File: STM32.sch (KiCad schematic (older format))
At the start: 46 parts, among them J1 Conn_02x05_Odd_Even, J2 Conn_02x03_Odd_Even, J3 Conn_01x30_Male, J4 Conn_02x03_Odd_Even, J5 Conn_01x30_Male, SW1 SW_Push, SW2 SW_Push, SW3 SW_Push, U1 LD1117S33TR_SOT223, U2 STM32F091RCTx, X1 32.768kHz(12.5pF), X2 8MHz(20pF)

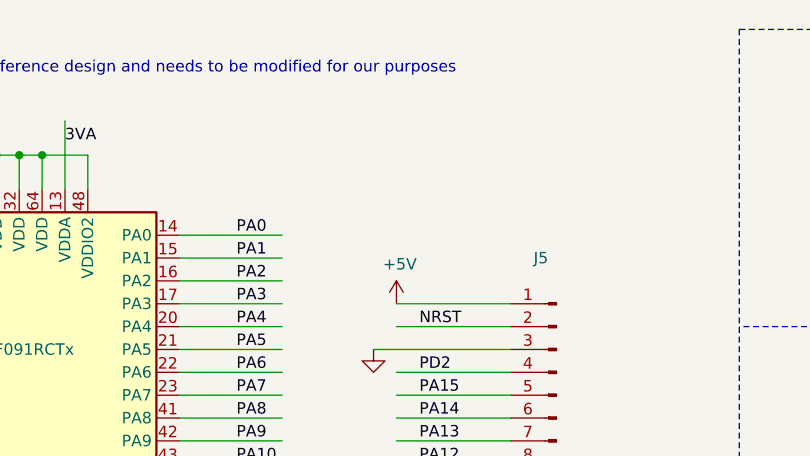
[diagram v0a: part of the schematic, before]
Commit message: updated the readme and added example of heirarchical labels
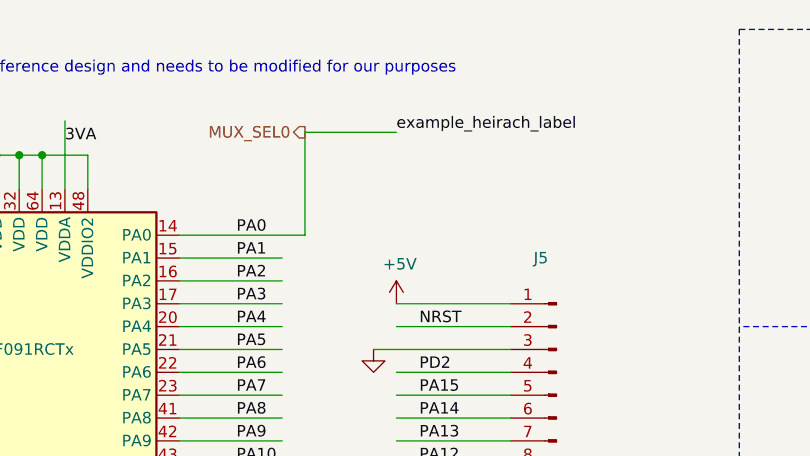
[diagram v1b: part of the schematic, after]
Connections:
- net labels added: MUX_SEL0, example_heirach_label
- wire segments 206 -> 208
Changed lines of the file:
@@
 $EndComp
-Wire Wire Line
-	6800 1650 7250 1650
 Wire Wire Line
 	6800 1750 7250 1750
@@
 Text Notes 4550 950  0    50   ~ 0
 TODO: This was copied for the ECE 362 Reference design and needs to be modified for our purposes
+Text HLabel 7350 1200 0    50   Output ~ 0
+MUX_SEL0
+Text Label 7750 1200 0    50   ~ 0
+example_heirach_label
+Wire Wire Line
+	7350 1200 7350 1650
+Wire Wire Line
+	6800 1650 7350 1650
+Wire Wire Line
+	7350 1200 7750 1200
 $EndSCHEMATC

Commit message: first iteration of main pcb
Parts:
- renumbered C9 to C10, C10 to C11, C11 to C12, C12 to C13, C13 to C14, C14 to C15, C1 to C2, C2 to C3, C3 to C4, C4 to C5, C5 to C6, C6 to C7, C7 to C8, C8 to C9, D1 to D2, D2 to D3, J1 to J5, J2 to J6, J3 to J7, J4 to J8, J5 to J9, R6 to R10, R7 to R11, R8 to R12, R9 to R13, R10 to R14, R11 to R15, R1 to R5, R2 to R6, R3 to R7, R4 to R8, R5 to R9, U1 to U4, U2 to U5
